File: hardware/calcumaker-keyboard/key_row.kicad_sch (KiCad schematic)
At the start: 30 parts, among them SW1 MX, SW10 MX, SW2 MX, SW3 MX, SW4 MX, SW5 MX, SW6 MX, SW7 MX, SW8 MX, SW9 MX

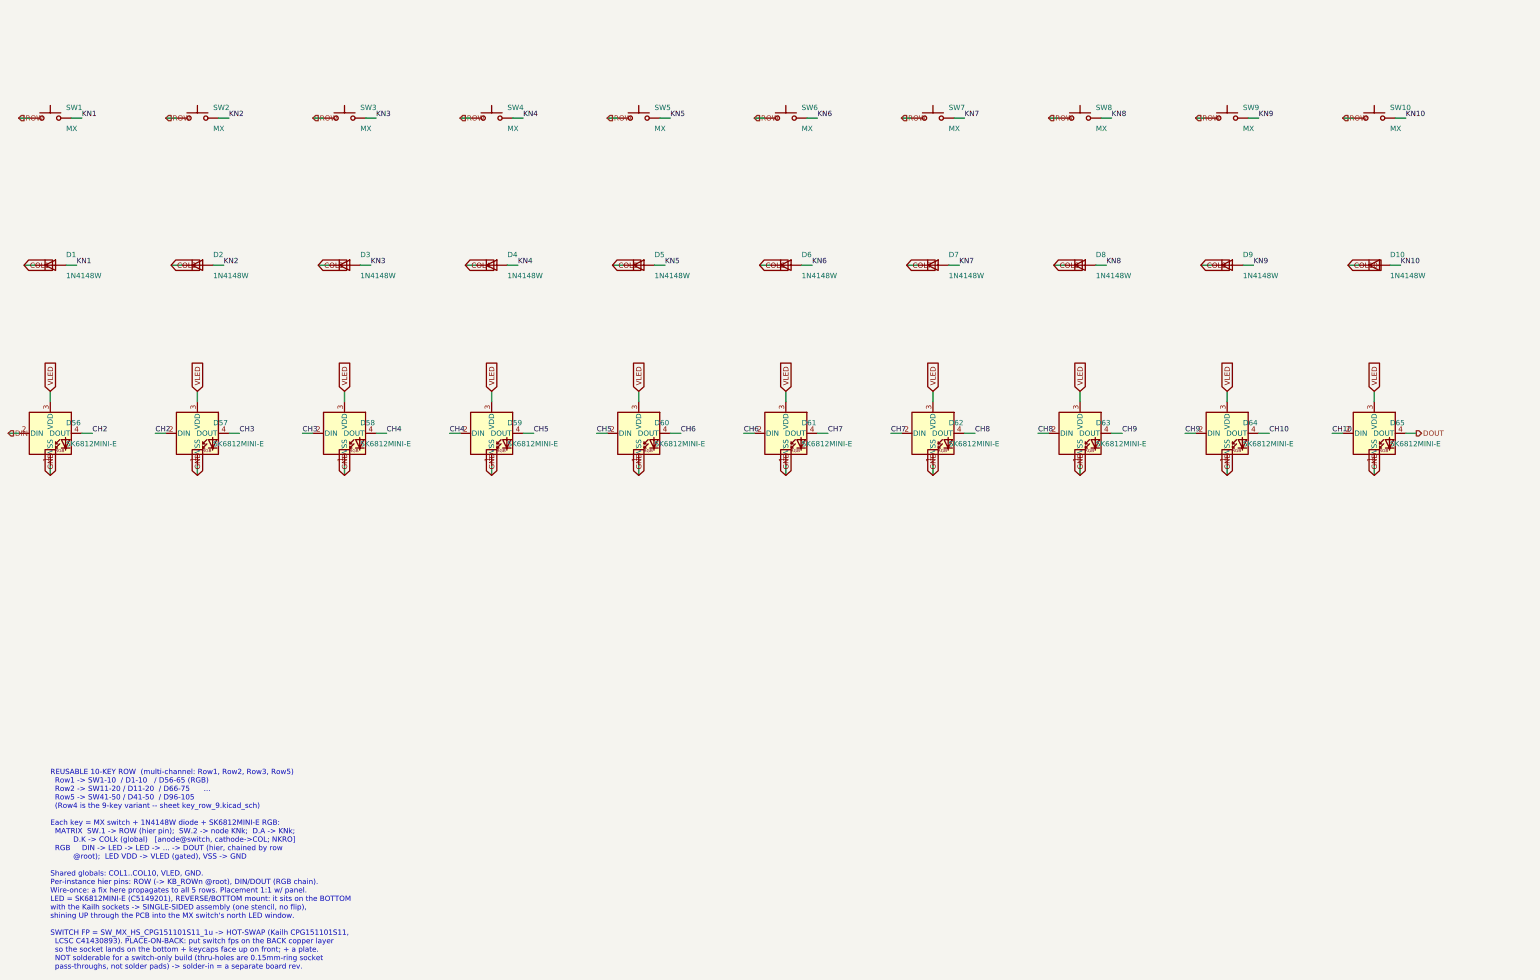
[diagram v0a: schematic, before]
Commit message: Wire mainboard and keypad schematics and verify expanded nets
Connect hierarchical interfaces, power/control circuits, debug links, matrix and RGB chains. Correct MCU package pins, diode polarity and power configuration; add bypass components and repeatable KiCad netlist/ERC checks. Document pin maps and remaining physical validation.
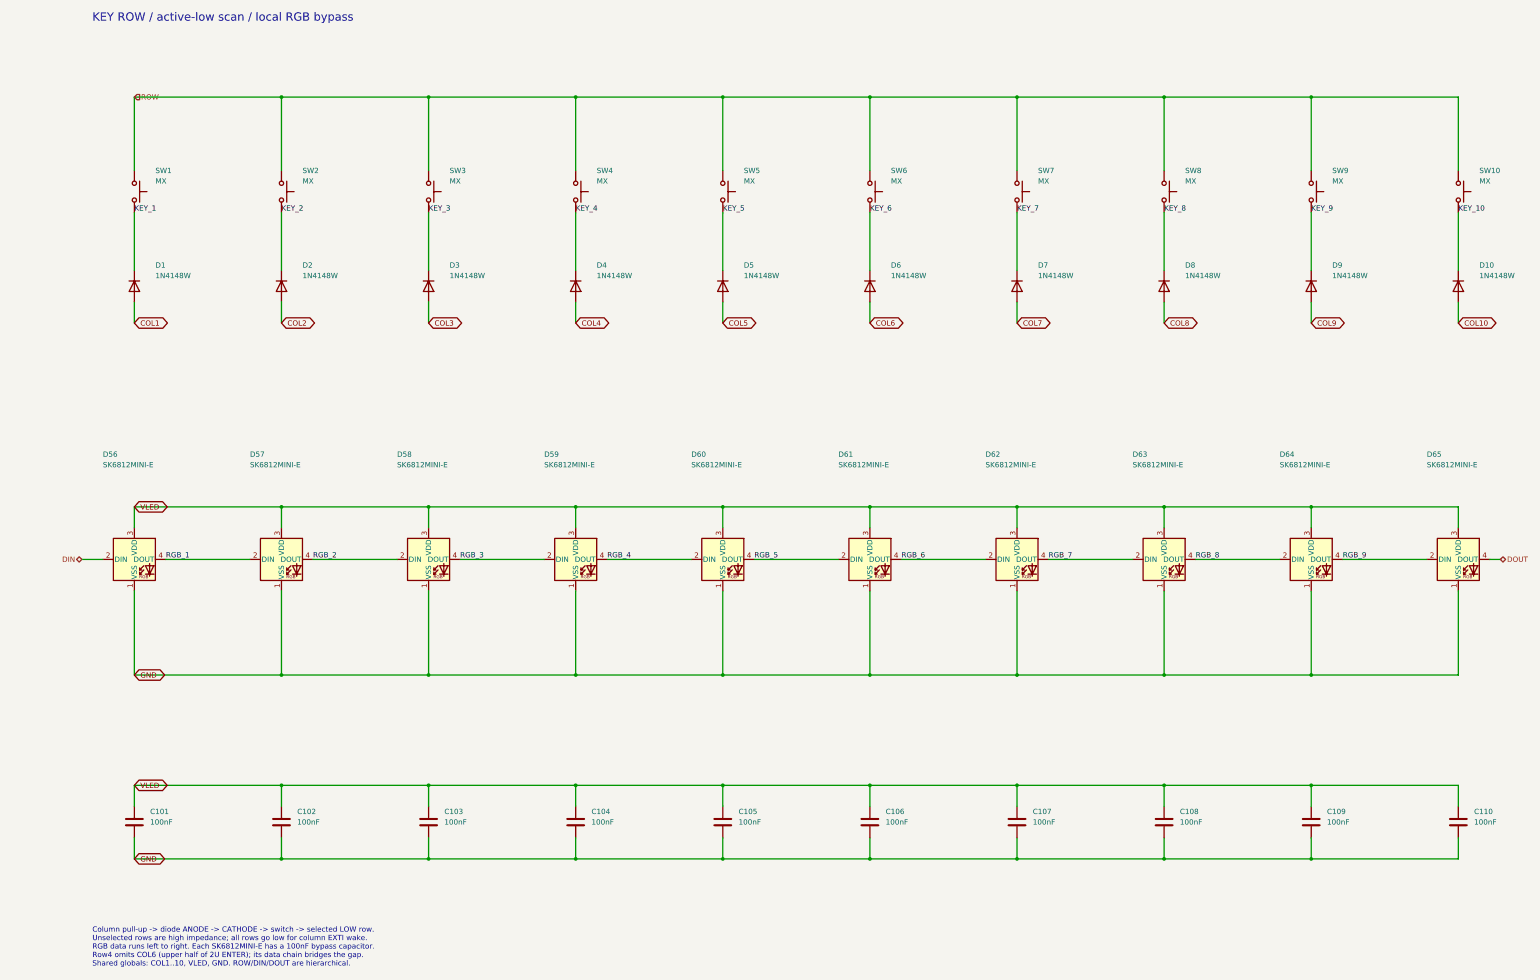
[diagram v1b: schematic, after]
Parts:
- added C101, C102, C103, C104, C105, C106, C107, C108, C109, C110: 100nF, Capacitor_SMD:C_0402_1005Metric, symbol Device:C
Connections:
- net COL1: now also D1.2 (A); no longer D1.1 (K)
- net COL10: now also D10.2 (A); no longer D10.1 (K)
- net COL2: now also D2.2 (A); no longer D2.1 (K)
- net COL3: now also D3.2 (A); no longer D3.1 (K)
- net COL4: now also D4.2 (A); no longer D4.1 (K)
- net COL5: now also D5.2 (A); no longer D5.1 (K)
- net COL6: now also D6.2 (A); no longer D6.1 (K)
- net COL7: now also D7.2 (A); no longer D7.1 (K)
- net COL8: now also D8.2 (A); no longer D8.1 (K)
- net COL9: now also D9.2 (A); no longer D9.1 (K)
- net GND: now also C101.2, C102.2, C103.2, C104.2, C105.2, C106.2, C107.2, C108.2, C109.2, C110.2
- net VLED: now also C101.1, C102.1, C103.1, C104.1, C105.1, C106.1, C107.1, C108.1, C109.1, C110.1
- net CH10 renamed RGB_9
- net CH2 renamed RGB_1
- net CH3 renamed RGB_2
- net CH4 renamed RGB_3
- net CH5 renamed RGB_4
- net CH6 renamed RGB_5
- net CH7 renamed RGB_6
- net CH8 renamed RGB_7
- net CH9 renamed RGB_8
- net KN1 renamed KEY_1
- net KEY_1: now also D1.1 (K); no longer D1.2 (A)
- net KN10 renamed KEY_10
- net KEY_10: now also D10.1 (K); no longer D10.2 (A)
- net KN2 renamed KEY_2
- net KEY_2: now also D2.1 (K); no longer D2.2 (A)
- net KN3 renamed KEY_3
- net KEY_3: now also D3.1 (K); no longer D3.2 (A)
- net KN4 renamed KEY_4
- net KEY_4: now also D4.1 (K); no longer D4.2 (A)
- net KN5 renamed KEY_5
- net KEY_5: now also D5.1 (K); no longer D5.2 (A)
- net KN6 renamed KEY_6
- net KEY_6: now also D6.1 (K); no longer D6.2 (A)
- net KN7 renamed KEY_7
- net KEY_7: now also D7.1 (K); no longer D7.2 (A)
- net KN8 renamed KEY_8
- net KEY_8: now also D8.1 (K); no longer D8.2 (A)
- net KN9 renamed KEY_9
- net KEY_9: now also D9.1 (K); no longer D9.2 (A)
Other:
- note added: "Column pull-up -> diode ANODE -> CATHODE -> switch -> selected LOW row. Unselected rows are high impedance; all rows go low for column EXTI wake. RGB data runs left to right. Each SK6812MINI-E has a 100nF bypass capacitor. Row4 omits COL6 (upper half of 2U ENTER); its data chain bridges the gap. Shared globals: COL1..10, VLED, GND. ROW/DIN/DOUT are hierarchical."
- note added: "KEY ROW / active-low scan / local RGB bypass"
- note removed: "REUSABLE 10-KEY ROW (multi-channel: Row1, Row2, Row3, Row5) Row1 -> SW1-10 / D1-10 / D56-65 (RGB) Row2 -> SW11-20 / D11-20 / D66-75 ... Row5 -> SW41-50 / D41-50 / D96-105 (Row4 is the 9-key variant -- sheet key_row_9.kicad_sch) Each key = MX switch + 1N4148W diode + SK6812MINI-E RGB: MATRIX SW.1 -> ROW (hier pin); SW.2 -> node KNk; D.A -> KNk; D.K -> COLk (global) [anode@switch, cathode->COL; NKR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"
- title: Calcumaker 16 — Keyboard — Reusable 10-key row (MX + diode + SK6812MINI-E RGB) -> Calcumaker 16 / keyboard / key row
- moved on the sheet: D1, D10, D2, D3, D4, D5, D56, D57, D58, D59, D6, D60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
